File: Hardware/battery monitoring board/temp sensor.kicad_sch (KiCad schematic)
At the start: 11 parts, among them J4 Conn_01x02, U1 MAX31855KASA

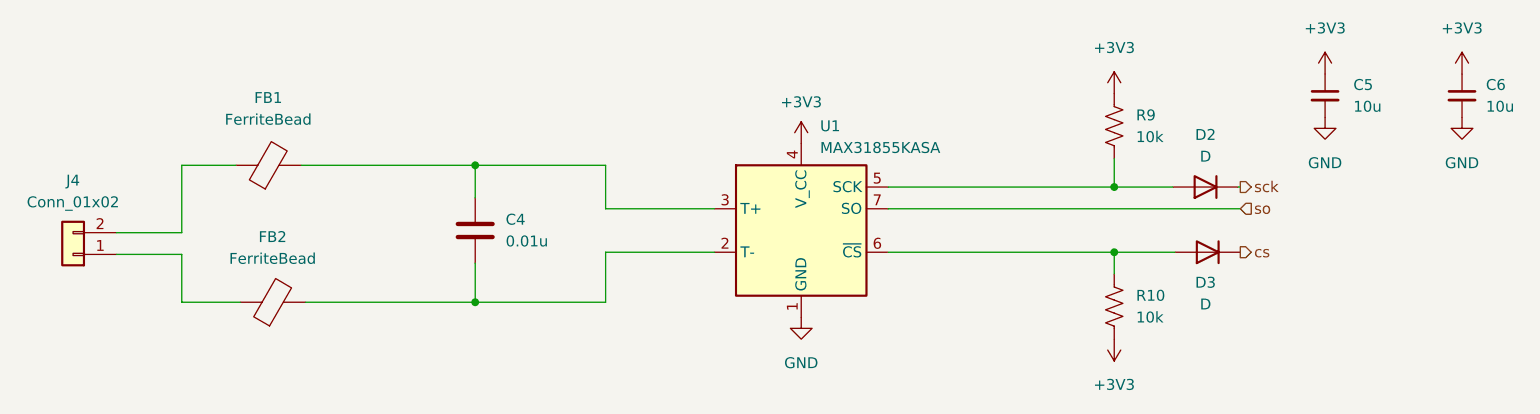
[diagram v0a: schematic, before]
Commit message: added test points (battery monitoring)
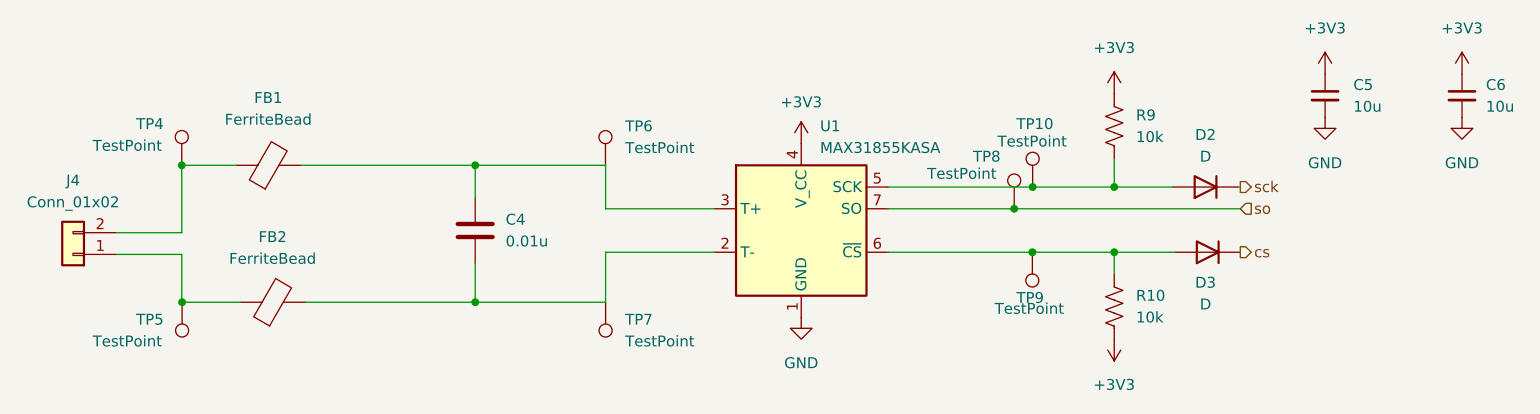
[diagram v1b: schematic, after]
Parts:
- added TP10, TP4, TP5, TP6, TP7, TP8, TP9: TestPoint, symbol Connector:TestPoint
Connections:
- net so: now also TP8.1
- net at FB1.1, J4.2 (Pin_2): now also TP4.1
- net at FB2.1, J4.1 (Pin_1): now also TP5.1
- net at D2.2 (A), R9.2, U1.5 (SCK): now also TP10.1
- net at D3.2 (A), R10.1, U1.6 (~{CS}): now also TP9.1
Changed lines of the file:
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@@
 (kicad_sch (version 20230121) (generator eeschema)
   (paper "A4")
+  (junction (at 68.834 91.186) (diameter 0) (color 0 0 0 0)
+  )
   (junction (at 103.124 91.186) (diameter 0) (color 0 0 0 0)
   )
+  (junction (at 168.2646 93.726) (diameter 0) (color 0 0 0 0)
+  )
   (junction (at 177.8 101.346) (diameter 0) (color 0 0 0 0)
   )
+  (junction (at 168.2309 101.346) (diameter 0) (color 0 0 0 0)
+  )
+  (junction (at 166.1092 96.266) (diameter 0) (color 0 0 0 0)
+  )
+  (junction (at 68.8733 107.188) (diameter 0) (color 0 0 0 0)
+  )
   (junction (at 103.124 107.188) (diameter 0) (color 0 0 0 0)
   )
@@
     (stroke (width 0) (type default))
   )
-  (wire (pts (xy 68.834 107.188) (xy 75.692 107.188))
-    (stroke (width 0) (type default))
-  )
-  (wire (pts (xy 151.384 101.346) (xy 177.8 101.346))
+  (wire (pts (xy 68.834 107.188) (xy 68.8733 107.188))
+    (stroke (width 0) (type default))
+  )
+  (wire (pts (xy 68.8733 107.188) (xy 75.692 107.188))
+    (stroke (width 0) (type default))
+  )
+  (wire (pts (xy 151.384 101.346) (xy 168.2309 101.346))
     (stroke (width 0) (type default))
   )
@@
     (stroke (width 0) (type default))
   )
-  (wire (pts (xy 151.384 93.726) (xy 177.8 93.726))
+  (wire (pts (xy 151.384 93.726) (xy 168.2646 93.726))
     (stroke (width 0) (type default))
   )
@@
     (stroke (width 0) (type default))
   )
+  (wire (pts (xy 168.2309 101.346) (xy 177.8 101.346))
+    (stroke (width 0) (type default))
+  )
   (wire (pts (xy 68.834 99.06) (xy 68.834 91.186))
     (stroke (width 0) (type default))
   )
+  (wire (pts (xy 103.124 91.186) (xy 103.124 94.996))
+    (stroke (width 0) (type default))
+  )
+  (wire (pts (xy 118.364 107.188) (xy 118.364 101.346))
+    (stroke (width 0) (type default))
+  )
+  (wire (pts (xy 83.312 107.188) (xy 103.124 107.188))
+    (stroke (width 0) (type default))
+  )
+  (wire (pts (xy 118.364 91.186) (xy 118.364 96.266))
+    (stroke (width 0) (type default))
+  )
+  (wire (pts (xy 118.364 101.346) (xy 131.064 101.346))
+    (stroke (width 0) (type default))
+  )
   (wire (pts (xy 61.214 99.06) (xy 68.834 99.06))
     (stroke (width 0) (type default))
   )
-  (wire (pts (xy 103.124 91.186) (xy 103.124 94.996))
-    (stroke (width 0) (type default))
-  )
-  (wire (pts (xy 118.364 107.188) (xy 118.364 101.346))
-    (stroke (width 0) (type default))
-  )
-  (wire (pts (xy 83.312 107.188) (xy 103.124 107.188))
-    (stroke (width 0) (type default))
-  )
-  (wire (pts (xy 118.364 91.186) (xy 118.364 96.266))
-    (stroke (width 0) (type default))
-  )
-  (wire (pts (xy 118.364 101.346) (xy 131.064 101.346))
-    (stroke (width 0) (type default))
-  )
   (wire (pts (xy 118.364 96.266) (xy 131.064 96.266))
     (stroke (width 0) (type default))
@@
     (stroke (width 0) (type default))
   )
+  (wire (pts (xy 166.1092 96.266) (xy 192.532 96.266))
+    (stroke (width 0) (type default))
+  )
   (wire (pts (xy 103.124 107.188) (xy 118.364 107.188))
     (stroke (width 0) (type default))
   )
-  (wire (pts (xy 151.384 96.266) (xy 192.532 96.266))
+  (wire (pts (xy 151.384 96.266) (xy 166.1092 96.266))
+    (stroke (width 0) (type default))
+  )
+  (wire (pts (xy 168.2646 93.726) (xy 177.8 93.726))
     (stroke (width 0) (type default))
   )
@@
     (effects (font (size 1.27 1.27)) (justify left))
   )
+  (symbol (lib_id "Connector:TestPoint") (at 68.8733 107.188 180) (unit 1)
+    (in_bom yes) (on_board yes) (dnp no)
+    (property "Reference" "TP5" (at 63.5 109.22 0)
+      (effects (font (size 1.27 1.27)) (justify right))
+    )
+    (property "Value" "TestPoint" (at 58.42 111.76 0)
+      (effects (font (size 1.27 1.27)) (justify right))
+    )
+    (property "Footprint" "" (at 63.7933 107.188 0)
+      (effects (font (size 1.27 1.27)) hide)
+    )
+    (property "Datasheet" "~" (at 63.7933 107.188 0)
+      (effects (font (size 1.27 1.27)) hide)
+    )
+    (pin "1")
+    (instances
+      (project "battery monitoring board"
+        (path "/bf623d80-ca5a-491f-9daa-4dffbeba5279/5ec2dbdf-a276-4d4c-99fc-008475c1e770"
+          (reference "TP5") (unit 1)
+        )
+      )
+    )
+  )
   (symbol (lib_id "Device:FerriteBead") (at 78.994 91.186 90) (unit 1)
     (in_bom yes) (on_board yes) (dnp no) (fields_autoplaced)
@@
     )
   )
+  (symbol (lib_id "Connector:TestPoint") (at 118.3621 107.1916 180) (unit 1)
+    (in_bom yes) (on_board yes) (dnp no) (fields_autoplaced)
+    (property "Reference" "TP7" (at 120.65 109.2236 0)
+      (effects (font (size 1.27 1.27)) (justify right))
+    )
+    (property "Value" "TestPoint" (at 120.65 111.7636 0)
+      (effects (font (size 1.27 1.27)) (justify right))
+    )
+    (property "Footprint" "" (at 113.2821 107.1916 0)
+      (effects (font (size 1.27 1.27)) hide)
+    )
+    (property "Datasheet" "~" (at 113.2821 107.1916 0)
+      (effects (font (size 1.27 1.27)) hide)
+    )
+    (pin "1")
+    (instances
+      (project "battery monitoring board"
+        (path "/bf623d80-ca5a-491f-9daa-4dffbeba5279/5ec2dbdf-a276-4d4c-99fc-008475c1e770"
+          (reference "TP7") (unit 1)
+        )
+      )
+    )
+  )
+  (symbol (lib_id "Connector:TestPoint") (at 68.834 91.186 0) (unit 1)
+    (in_bom yes) (on_board yes) (dnp no)
+    (property "Reference" "TP4" (at 63.5 86.36 0)
+      (effects (font (size 1.27 1.27)) (justify left))
+    )
+    (property "Value" "TestPoint" (at 58.42 88.9 0)
+      (effects (font (size 1.27 1.27)) (justify left))
+    )
+    (property "Footprint" "" (at 73.914 91.186 0)
+      (effects (font (size 1.27 1.27)) hide)
+    )
+    (property "Datasheet" "~" (at 73.914 91.186 0)
+      (effects (font (size 1.27 1.27)) hide)
+    )
+    (pin "1")
+    (instances
+      (project "battery monitoring board"
+        (path "/bf623d80-ca5a-491f-9daa-4dffbeba5279/5ec2dbdf-a276-4d4c-99fc-008475c1e770"
+          (reference "TP4") (unit 1)
+        )
+      )
+    )
+  )
+  (symbol (lib_id "Connector:TestPoint") (at 166.1092 96.266 0) (unit 1)
+    (in_bom yes) (on_board yes) (dnp no)
+    (property "Reference" "TP8" (at 161.29 90.17 0)
+      (effects (font (size 1.27 1.27)) (justify left))
+    )
+    (property "Value" "TestPoint" (at 155.9382 92.1753 0)
+      (effects (font (size 1.27 1.27)) (justify left))
+    )
+    (property "Footprint" "" (at 171.1892 96.266 0)
+      (effects (font (size 1.27 1.27)) hide)
+    )
+    (property "Datasheet" "~" (at 171.1892 96.266 0)
+      (effects (font (size 1.27 1.27)) hide)
+    )
+    (pin "1")
+    (instances
+      (project "battery monitoring board"
+        (path "/bf623d80-ca5a-491f-9daa-4dffbeba5279/5ec2dbdf-a276-4d4c-99fc-008475c1e770"
+          (reference "TP8") (unit 1)
+        )
+      )
+    )
+  )
+  (symbol (lib_id "Connector:TestPoint") (at 168.2309 101.346 180) (unit 1)
+    (in_bom yes) (on_board yes) (dnp no)
+    (property "Reference" "TP9" (at 166.37 106.68 0)
+      (effects (font (size 1.27 1.27)) (justify right))
+    )
+    (property "Value" "TestPoint" (at 163.83 107.95 0)
+      (effects (font (size 1.27 1.27)) (justify right))
+    )
+    (property "Footprint" "" (at 163.1509 101.346 0)
+      (effects (font (size 1.27 1.27)) hide)
+    )
+    (property "Datasheet" "~" (at 163.1509 101.346 0)
+      (effects (font (size 1.27 1.27)) hide)
+    )
+    (pin "1")
+    (instances
+      (project "battery monitoring board"
+        (path "/bf623d80-ca5a-491f-9daa-4dffbeba5279/5ec2dbdf-a276-4d4c-99fc-008475c1e770"
+          (reference "TP9") (unit 1)
+        )
+      )
+    )
+  )
   (symbol (lib_id "Device:R_US") (at 177.8 107.696 0) (unit 1)
     (in_bom yes) (on_board yes) (dnp no) (fields_autoplaced)
@@
         (path "/bf623d80-ca5a-491f-9daa-4dffbeba5279/5ec2dbdf-a276-4d4c-99fc-008475c1e770"
           (reference "C6") (unit 1)
+        )
+      )
+    )
+  )
+  (symbol (lib_id "Connector:TestPoint") (at 118.3471 91.1982 0) (unit 1)
+    (in_bom yes) (on_board yes) (dnp no) (fields_autoplaced)
+    (property "Reference" "TP6" (at 120.65 86.6262 0)
+      (effects (font (size 1.27 1.27)) (justify left))
+    )
+    (property "Value" "TestPoint" (at 120.65 89.1662 0)
+      (effects (font (size 1.27 1.27)) (justify left))
+    )
+    (property "Footprint" "" (at 123.4271 91.1982 0)
+      (effects (font (size 1.27 1.27)) hide)
+    )
+    (property "Datasheet" "~" (at 123.4271 91.1982 0)
+      (effects (font (size 1.27 1.27)) hide)
+    )
+    (pin "1")
+    (instances
+      (project "battery monitoring board"
+        (path "/bf623d80-ca5a-491f-9daa-4dffbeba5279/5ec2dbdf-a276-4d4c-99fc-008475c1e770"
+          (reference "TP6") (unit 1)
         )
       )
@@
         )
       )
+    )
+  )
+  (symbol (lib_id "Connector:TestPoint") (at 168.2646 93.726 0) (unit 1)
+    (in_bom yes) (on_board yes) (dnp no)
+    (property "Reference" "TP10" (at 166.37 86.36 0)
+      (effects (font (size 1.27 1.27)) (justify left))
+    )
+    (property "Value" "TestPoint" (at 164.1558 88.4033 0)
+      (effects (font (size 1.27 1.27)) (justify left))
+    )
+    (property "Footprint" "" (at 173.3446 93.726 0)
+      (effects (font (size 1.27 1.27)) hide)
+    )
+    (property "Datasheet" "~" (at 173.3446 93.726 0)
+      (effects (font (size 1.27 1.27)) hide)
+    )
+    (pin "1")
+    (instances
+      (project "battery monitoring board"
+        (path "/bf623d80-ca5a-491f-9daa-4dffbeba5279/5ec2dbdf-a276-4d4c-99fc-008475c1e770"
+          (reference "TP10") (unit 1)
+        )
+      )

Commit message: Added footprints to battery monitoring
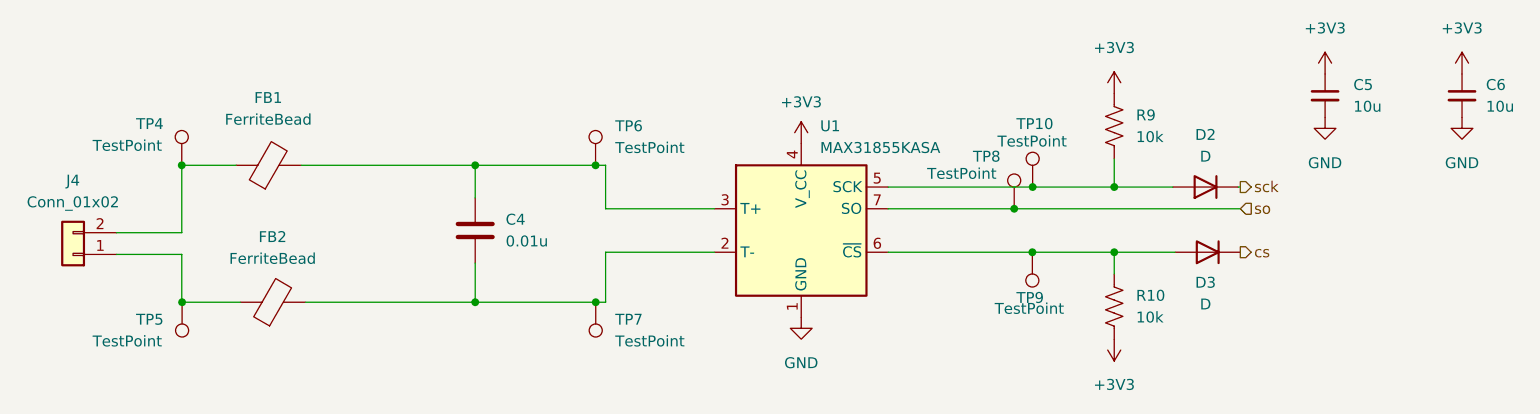
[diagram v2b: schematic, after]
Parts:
- C4, C5, C6: footprint (none) -> Capacitor_SMD:C_0805_2012Metric_Pad1.18x1.45mm_HandSolder
- D2, D3: footprint (none) -> Diode_SMD:D_0805_2012Metric_Pad1.15x1.40mm_HandSolder
- FB1, FB2: footprint (none) -> Ferrite_SMD_AKL:Ferrite_0805_2012Metric_Pad1.05x1.20mm_BigPads
- J4: footprint 4ms_Connector:Pins_1x02_2.54mm_TH -> Library:TE_282836-2
- R10, R9: footprint (none) -> Resistor_SMD:R_0805_2012Metric_Pad1.20x1.40mm_HandSolder
- TP10, TP4, TP5, TP6, TP7, TP8, TP9: footprint (none) -> Library:Test Pads
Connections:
- net at C4.1, FB1.2, U1.3 (T+): now also TP6.1
- net at C4.2, FB2.2, U1.2 (T-): now also TP7.1
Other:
- moved on the sheet: TP6, TP7
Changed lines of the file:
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@@
   (junction (at 168.2646 93.726) (diameter 0) (color 0 0 0 0)
   )
+  (junction (at 117.1908 91.186) (diameter 0) (color 0 0 0 0)
+  )
   (junction (at 177.8 101.346) (diameter 0) (color 0 0 0 0)
   )
@@
   (junction (at 103.124 107.188) (diameter 0) (color 0 0 0 0)
   )
+  (junction (at 117.2073 107.188) (diameter 0) (color 0 0 0 0)
+  )
   (junction (at 177.8 93.726) (diameter 0) (color 0 0 0 0)
   )
@@
     (stroke (width 0) (type default))
   )
+  (wire (pts (xy 117.1908 91.186) (xy 118.364 91.186))
+    (stroke (width 0) (type default))
+  )
   (wire (pts (xy 118.364 101.346) (xy 131.064 101.346))
     (stroke (width 0) (type default))
@@
     (stroke (width 0) (type default))
   )
+  (wire (pts (xy 117.2073 107.188) (xy 118.364 107.188))
+    (stroke (width 0) (type default))
+  )
   (wire (pts (xy 118.364 96.266) (xy 131.064 96.266))
     (stroke (width 0) (type default))
@@
     (stroke (width 0) (type default))
   )
-  (wire (pts (xy 103.124 107.188) (xy 118.364 107.188))
+  (wire (pts (xy 103.124 107.188) (xy 117.2073 107.188))
     (stroke (width 0) (type default))
   )
@@
     (stroke (width 0) (type default))
   )
-  (wire (pts (xy 103.124 91.186) (xy 118.364 91.186))
+  (wire (pts (xy 103.124 91.186) (xy 117.1908 91.186))
     (stroke (width 0) (type default))
   )
@@
       (effects (font (size 1.27 1.27)) (justify right))
     )
-    (property "Footprint" "" (at 63.7933 107.188 0)
+    (property "Footprint" "Library:Test Pads" (at 63.7933 107.188 0)
       (effects (font (size 1.27 1.27)) hide)
     )
@@
       (effects (font (size 1.27 1.27)))
     )
-    (property "Footprint" "" (at 78.994 92.964 90)
+    (property "Footprint" "Ferrite_SMD_AKL:Ferrite_0805_2012Metric_Pad1.05x1.20mm_BigPads" (at 78.994 92.964 90)
       (effects (font (size 1.27 1.27)) hide)
     )
@@
       (effects (font (size 1.27 1.27)))
     )
-    (property "Footprint" "" (at 79.502 108.966 90)
+    (property "Footprint" "Ferrite_SMD_AKL:Ferrite_0805_2012Metric_Pad1.05x1.20mm_BigPads" (at 79.502 108.966 90)
       (effects (font (size 1.27 1.27)) hide)
     )
@@
       (effects (font (size 1.27 1.27)) (justify left))
     )
-    (property "Footprint" "" (at 178.816 86.868 90)
+    (property "Footprint" "Resistor_SMD:R_0805_2012Metric_Pad1.20x1.40mm_HandSolder" (at 178.816 86.868 90)
       (effects (font (size 1.27 1.27)) hide)
     )
@@
     )
   )
-  (symbol (lib_id "Connector:TestPoint") (at 118.3621 107.1916 180) (unit 1)
-    (in_bom yes) (on_board yes) (dnp no) (fields_autoplaced)
-    (property "Reference" "TP7" (at 120.65 109.2236 0)
+  (symbol (lib_id "Connector:TestPoint") (at 117.2073 107.188 180) (unit 1)
+    (in_bom yes) (on_board yes) (dnp no) (fields_autoplaced)
+    (property "Reference" "TP7" (at 119.4952 109.22 0)
       (effects (font (size 1.27 1.27)) (justify right))
     )
-    (property "Value" "TestPoint" (at 120.65 111.7636 0)
+    (property "Value" "TestPoint" (at 119.4952 111.76 0)
       (effects (font (size 1.27 1.27)) (justify right))
     )
-    (property "Footprint" "" (at 113.2821 107.1916 0)
-      (effects (font (size 1.27 1.27)) hide)
-    )
-    (property "Datasheet" "~" (at 113.2821 107.1916 0)
+    (property "Footprint" "Library:Test Pads" (at 112.1273 107.188 0)
+      (effects (font (size 1.27 1.27)) hide)
+    )
+    (property "Datasheet" "~" (at 112.1273 107.188 0)
       (effects (font (size 1.27 1.27)) hide)
     )
@@
       (effects (font (size 1.27 1.27)) (justify left))
     )
-    (property "Footprint" "" (at 73.914 91.186 0)
+    (property "Footprint" "Library:Test Pads" (at 73.914 91.186 0)
       (effects (font (size 1.27 1.27)) hide)
     )
@@
       (effects (font (size 1.27 1.27)) (justify left))
     )
-    (property "Footprint" "" (at 171.1892 96.266 0)
+    (property "Footprint" "Library:Test Pads" (at 171.1892 96.266 0)
       (effects (font (size 1.27 1.27)) hide)
     )
@@
       (effects (font (size 1.27 1.27)) (justify right))
     )
-    (property "Footprint" "" (at 163.1509 101.346 0)
+    (property "Footprint" "Library:Test Pads" (at 163.1509 101.346 0)
       (effects (font (size 1.27 1.27)) hide)
     )
@@
       (effects (font (size 1.27 1.27)) (justify left))
     )
-    (property "Footprint" "" (at 178.816 107.95 90)
+    (property "Footprint" "Resistor_SMD:R_0805_2012Metric_Pad1.20x1.40mm_HandSolder" (at 178.816 107.95 90)
       (effects (font (size 1.27 1.27)) hide)
     )
@@
       (effects (font (size 1.27 1.27)) (justify left))
     )
-    (property "Footprint" "" (at 104.0892 102.616 0)
+    (property "Footprint" "Capacitor_SMD:C_0805_2012Metric_Pad1.18x1.45mm_HandSolder" (at 104.0892 102.616 0)
       (effects (font (size 1.27 1.27)) hide)
     )
@@
       (effects (font (size 1.27 1.27)) (justify left))
     )
-    (property "Footprint" "" (at 218.44 83.058 0)
+    (property "Footprint" "Capacitor_SMD:C_0805_2012Metric_Pad1.18x1.45mm_HandSolder" (at 218.44 83.058 0)
       (effects (font (size 1.27 1.27)) hide)
     )
@@
     )
   )
-  (symbol (lib_id "Connector:TestPoint") (at 118.3471 91.1982 0) (unit 1)
-    (in_bom yes) (on_board yes) (dnp no) (fields_autoplaced)
-    (property "Reference" "TP6" (at 120.65 86.6262 0)
-      (effects (font (size 1.27 1.27)) (justify left))
-    )
-    (property "Value" "TestPoint" (at 120.65 89.1662 0)
-      (effects (font (size 1.27 1.27)) (justify left))
-    )
-    (property "Footprint" "" (at 123.4271 91.1982 0)
-      (effects (font (size 1.27 1.27)) hide)
-    )
-    (property "Datasheet" "~" (at 123.4271 91.1982 0)
+  (symbol (lib_id "Connector:TestPoint") (at 117.1908 91.186 0) (unit 1)
+    (in_bom yes) (on_board yes) (dnp no) (fields_autoplaced)
+    (property "Reference" "TP6" (at 119.4937 86.614 0)
+      (effects (font (size 1.27 1.27)) (justify left))
+    )
+    (property "Value" "TestPoint" (at 119.4937 89.154 0)
+      (effects (font (size 1.27 1.27)) (justify left))
+    )
+    (property "Footprint" "Library:Test Pads" (at 122.2708 91.186 0)
+      (effects (font (size 1.27 1.27)) hide)
+    )
+    (property "Datasheet" "~" (at 122.2708 91.186 0)
       (effects (font (size 1.27 1.27)) hide)
     )
@@
       (effects (font (size 1.27 1.27)) (justify left))
     )
-    (property "Footprint" "" (at 202.438 83.058 0)
+    (property "Footprint" "Capacitor_SMD:C_0805_2012Metric_Pad1.18x1.45mm_HandSolder" (at 202.438 83.058 0)
       (effects (font (size 1.27 1.27)) hide)
     )
@@
       (effects (font (size 1.27 1.27)))
     )
-    (property "Footprint" "" (at 188.468 93.726 0)
+    (property "Footprint" "Diode_SMD:D_0805_2012Metric_Pad1.15x1.40mm_HandSolder" (at 188.468 93.726 0)
       (effects (font (size 1.27 1.27)) hide)
     )
@@
       (effects (font (size 1.27 1.27)) (justify left))
     )
-    (property "Footprint" "" (at 173.3446 93.726 0)
+    (property "Footprint" "Library:Test Pads" (at 173.3446 93.726 0)
       (effects (font (size 1.27 1.27)) hide)
     )
@@
       (effects (font (size 1.27 1.27)))
     )
-    (property "Footprint" "" (at 188.722 101.346 0)
+    (property "Footprint" "Diode_SMD:D_0805_2012Metric_Pad1.15x1.40mm_HandSolder" (at 188.722 101.346 0)
       (effects (font (size 1.27 1.27)) hide)
     )
@@
       (effects (font (size 1.27 1.27)))
     )
-    (property "Footprint" "4ms_Connector:Pins_1x02_2.54mm_TH" (at 56.769 106.045 0)
-      (effects (font (size 1.27 1.27)) hide)
-    )
+    (property "Footprint" "Library:TE_282836-2" (at 56.769 106.045 0)
+      (effects (font (size 1.27 1.27)) hide)
+    )

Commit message: updated battery board pt.II
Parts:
- J4: footprint Library:TE_282836-2 -> 4ms_Connector:Pins_1x02_2.54mm_TH
- TP10: renamed from TP9; footprint Library:Test Pads -> PCM_4ms_TestPoint:TestPoint_Pad_06
- TP11: renamed from TP10; footprint Library:Test Pads -> PCM_4ms_TestPoint:TestPoint_Pad_06
- TP5: renamed from TP4; footprint Library:Test Pads -> PCM_4ms_TestPoint:TestPoint_Pad_06
- TP6: renamed from TP5; footprint Library:Test Pads -> PCM_4ms_TestPoint:TestPoint_Pad_06
- TP7: renamed from TP6; footprint Library:Test Pads -> PCM_4ms_TestPoint:TestPoint_Pad_06
- TP8: renamed from TP7; footprint Library:Test Pads -> PCM_4ms_TestPoint:TestPoint_Pad_06
- TP9: renamed from TP8; footprint Library:Test Pads -> PCM_4ms_TestPoint:TestPoint_Pad_06
- renumbered C4 to C5, C5 to C6, C6 to C7, D2 to D4, D3 to D5, R9 to R11, R10 to R12
